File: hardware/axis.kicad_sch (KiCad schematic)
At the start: 43 parts, among them J101 Cortex_Debug, J102 DX07S016JA3, SW101 SKSG, SW102 SKSG, U101 TPS78433QWDRBRQ1, U102 ATSAMD51G, U103 BMM150, U104 BHI160, Y101 32k768

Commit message: Refresh
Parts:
- C102, C103, C104, C105, C111: Rating (none) -> 50V
- D103: Mouser 755-SML-D12M8WT86C -> 755-SML-D12D1WT86; Product SML-D12M8WT86C -> SML-D12D1WT86
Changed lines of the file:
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@@
 			)
 		)
+		(property "Rating" "50V"
+			(at 115.57 46.99 0)
+			(effects
+				(font
+					(size 1.27 1.27)
+				)
+				(hide yes)
+			)
+		)
 		(pin "1"
 		)
@@
 			)
 		)
+		(property "Rating" "50V"
+			(at 148.59 187.96 0)
+			(effects
+				(font
+					(size 1.27 1.27)
+				)
+				(hide yes)
+			)
+		)
 		(pin "1"
 		)
@@
 			)
 		)
-		(property "Mouser" "755-SML-D12M8WT86C"
+		(property "Mouser" "755-SML-D12D1WT86"
 			(at 254 97.536 0)
 			(effects
@@
 			)
 		)
-		(property "Product" "SML-D12M8WT86C "
+		(property "Product" "SML-D12D1WT86"
 			(at 127 41.91 0)
 			(effects
@@
 		(at 205.74 157.48 90)
 		(unit 1)
-		(exclude_from_sim no)
+		(exclude_from_sim yes)
 		(in_bom no)
 		(on_board yes)
@@
 			)
 		)
+		(property "Sim.Enable" "0"
+			(at 205.74 157.48 0)
+			(effects
+				(font
+					(size 1.27 1.27)
+				)
+				(hide yes)
+			)
+		)
 		(instances
 			(project "axis"
@@
 		(at 254 151.13 0)
 		(unit 1)
-		(exclude_from_sim no)
+		(exclude_from_sim yes)
 		(in_bom no)
 		(on_board yes)
@@
 			)
 		)
+		(property "Sim.Enable" "0"
+			(at 254 151.13 0)
+			(effects
+				(font
+					(size 1.27 1.27)
+				)
+				(hide yes)
+			)
+		)
 		(instances
 			(project ""
@@
 		(at 125.73 101.6 0)
 		(unit 1)
-		(exclude_from_sim no)
+		(exclude_from_sim yes)
 		(in_bom no)
 		(on_board yes)
@@
 			)
 		)
+		(property "Sim.Enable" "0"
+			(at 125.73 101.6 0)
+			(effects
+				(font
+					(size 1.27 1.27)
+				)
+				(hide yes)
+			)
+		)
 		(pin "1"
 		)
@@
 			)
 		)
-		(property "Description" "Power symbol creates a global label with name \"Earth\""
+		(property "Description" "Power symbol creates a global label with name \"Shield\""
 			(at 179.07 125.73 0)
 			(effects
@@
 			)
 		)
-		(property "Description" "Power symbol creates a global label with name \"Earth\""
+		(property "Description" "Power symbol creates a global label with name \"Shield\""
 			(at 238.76 81.28 0)
 			(effects
@@
 			)
 		)
+		(property "Rating" "50V"
+			(at 105.41 46.99 0)
+			(effects
+				(font
+					(size 1.27 1.27)
+				)
+				(hide yes)
+			)
+		)
 		(pin "1"
 		)
@@
 			)
 		)
+		(property "Rating" "50V"
+			(at 85.09 46.99 0)
+			(effects
+				(font
+					(size 1.27 1.27)
+				)
+				(hide yes)
+			)
+		)
 		(pin "1"
 		)
@@
 		(at 254 158.75 0)
 		(unit 1)
-		(exclude_from_sim no)
+		(exclude_from_sim yes)
 		(in_bom no)
 		(on_board yes)
@@
 			)
 		)
+		(property "Sim.Enable" "0"
+			(at 254 158.75 0)
+			(effects
+				(font
+					(size 1.27 1.27)
+				)
+				(hide yes)
+			)
+		)
 		(instances
 			(project "axis"
@@
 			)
 		)
+		(property "Rating" "50V"
+			(at 95.25 46.99 0)
+			(effects
+				(font
+					(size 1.27 1.27)
+				)
+				(hide yes)
+			)
+		)
 		(pin "1"
 		)
@@
 		(at 179.07 175.26 0)
 		(unit 1)
-		(exclude_from_sim no)
+		(exclude_from_sim yes)
 		(in_bom no)
 		(on_board yes)
@@
 			)
 		)
+		(property "Sim.Enable" "0"
+			(at 179.07 175.26 0)
+			(effects
+				(font
+					(size 1.27 1.27)
+				)
+				(hide yes)
+			)
+		)
 		(instances
 			(project "axis"
@@
 		(at 180.34 156.21 0)
 		(unit 1)
-		(exclude_from_sim no)
+		(exclude_from_sim yes)
 		(in_bom no)
 		(on_board yes)
@@
 			(at 180.34 156.21 0)
 			(effects
+				(font
+					(size 1.27 1.27)
+				)
+				(hide yes)
+			)
+		)
+		(property "Sim.Enable" "0"
+			(at 180.34 156.21 0)
+			(effects

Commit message: Refresh
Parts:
- C101, C110: Rating (none) -> 10V
- C102, C103, C104, C105, C111: Manufacturer YAGEO -> TDK; Mouser 603-CC603KRX7R9BB105 -> 810-CGA3E3X7R1H105K0; Product CC0603KRX7R9BB105 -> CGA3E3X7R1H105K080AB

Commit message: Update library
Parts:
- J101: value Cortex_Debug -> Cortex; footprint V2_Cortex_Debug:Cortex_Debug_Pad -> V2_Connector_Debug:Cortex; symbol V2_Cortex_Debug:Cortex_Debug -> V2_Connector_Debug:Cortex
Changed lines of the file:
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@@
 	)
 	(symbol
-		(lib_id "V2_Cortex_Debug:Cortex_Debug")
+		(lib_id "V2_Connector_Debug:Cortex")
 		(at 125.73 101.6 0)
 		(unit 1)
@@
 			)
 		)
-		(property "Value" "Cortex_Debug"
+		(property "Value" "Cortex"
 			(at 127 91.44 0)
 			(effects
@@
 			)
 		)
-		(property "Footprint" "V2_Cortex_Debug:Cortex_Debug_Pad"
+		(property "Footprint" "V2_Connector_Debug:Cortex"
 			(at 125.73 115.57 0)
 			(effects

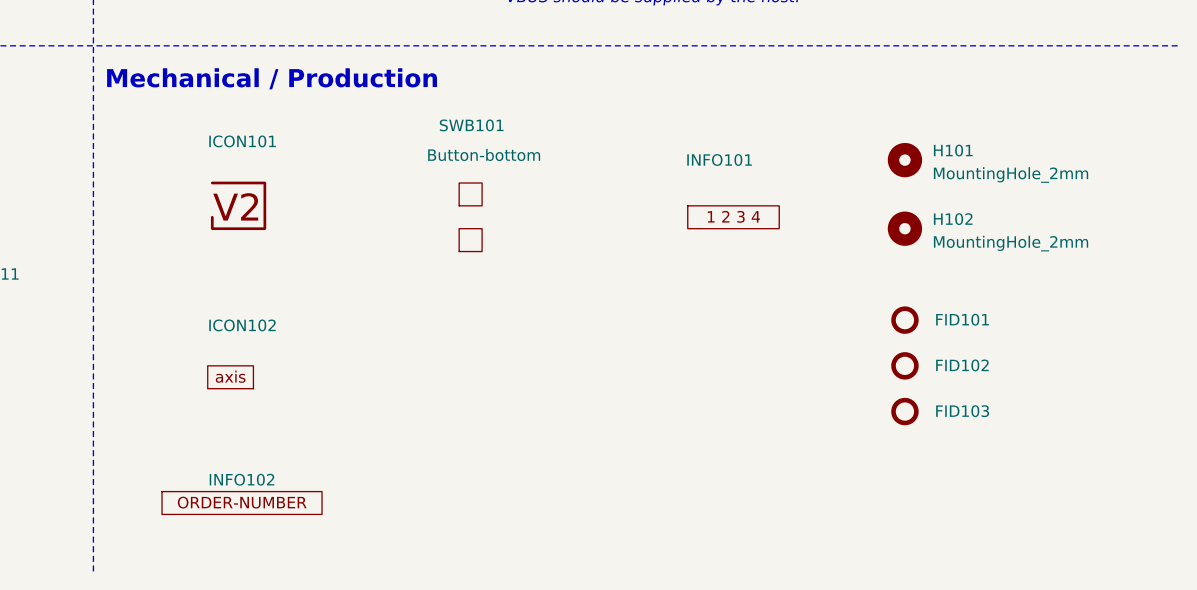
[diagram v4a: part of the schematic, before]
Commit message: Replace Order_Number
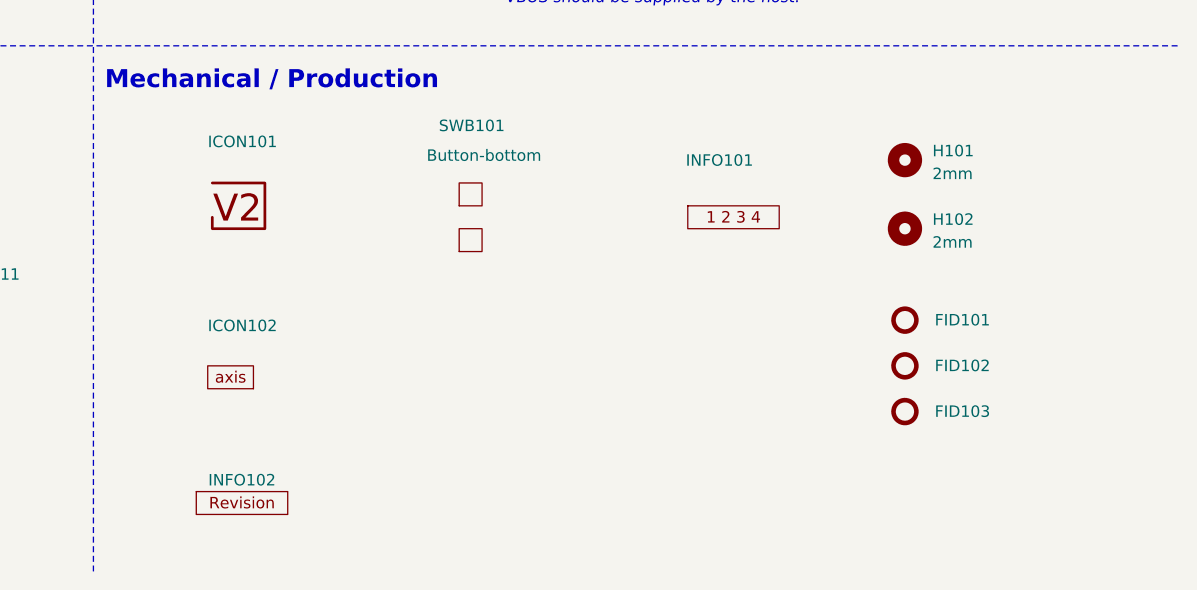
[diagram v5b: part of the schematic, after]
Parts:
- H101, H102: value MountingHole_2mm -> 2mm
- INFO102: value Order_Number -> ~; footprint V2_Production:Order_Number -> V2_Production:Revision; symbol V2_Production:Order_Number -> V2_Production:Revision
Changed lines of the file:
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@@
 		(at 205.74 157.48 90)
 		(unit 1)
-		(exclude_from_sim yes)
+		(exclude_from_sim no)
 		(in_bom no)
 		(on_board yes)
@@
 			)
 		)
+		(property "Sim.Enable" "0"
+			(at 205.74 157.48 0)
+			(effects
+				(font
+					(size 1.27 1.27)
+				)
+				(hide yes)
+			)
+		)
 		(instances
 			(project "axis"
@@
 		(at 254 151.13 0)
 		(unit 1)
-		(exclude_from_sim yes)
+		(exclude_from_sim no)
 		(in_bom no)
 		(on_board yes)
@@
 			)
 		)
-		(property "Value" "MountingHole_2mm"
+		(property "Value" "2mm"
 			(at 257.048 152.654 0)
 			(effects
@@
 	)
 	(symbol
-		(lib_id "V2_Production:Order_Number")
+		(lib_id "V2_Production:Revision")
 		(at 180.34 189.23 0)
 		(unit 1)
@@
 			)
 		)
-		(property "Value" "Order_Number"
+		(property "Value" "~"
 			(at 180.34 191.77 0)
 			(effects
@@
 			)
 		)
-		(property "Footprint" "V2_Production:Order_Number"
+		(property "Footprint" "V2_Production:Revision"
 			(at 180.34 194.31 0)
 			(effects
@@
 		(at 254 158.75 0)
 		(unit 1)
-		(exclude_from_sim yes)
+		(exclude_from_sim no)
 		(in_bom no)
 		(on_board yes)
@@
 			)
 		)
-		(property "Value" "MountingHole_2mm"
+		(property "Value" "2mm"
 			(at 257.048 160.274 0)
 			(effects
@@
 		(at 179.07 175.26 0)
 		(unit 1)
-		(exclude_from_sim yes)
+		(exclude_from_sim no)
 		(in_bom no)
 		(on_board yes)
@@
 			)
 		)
+		(property "Sim.Enable" "0"
+			(at 179.07 175.26 0)
+			(effects
+				(font
+					(size 1.27 1.27)
+				)
+				(hide yes)
+			)
+		)
 		(instances
 			(project "axis"
@@
 		(at 180.34 156.21 0)
 		(unit 1)
-		(exclude_from_sim yes)
+		(exclude_from_sim no)
 		(in_bom no)
 		(on_board yes)

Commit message: Update Library
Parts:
- C101, C110: symbol V2_Device:C_0603_10u -> V2_Capacitor:0603_10u
- C102, C103, C104, C105, C111: symbol V2_Device:C_0603_1u -> V2_Capacitor:0603_1u
- C106, C107: symbol V2_Device:C_0805_10u -> V2_Capacitor:0805_10u
- C108, C109: symbol V2_Device:C_0603_18p -> V2_Capacitor:0603_18p
- C112: symbol V2_Device:C_0603_0u47 -> V2_Capacitor:0603_0u47
- D103: symbol V2_Device:LED_0603_Orange -> V2_LED:0603_Orange
- R101: symbol V2_Device:R_0603_330R -> V2_Resistor:0603_330R
- R102, R103: symbol V2_Device:R_0603_5k1 -> V2_Resistor:0603_5k1
- R104: symbol V2_Device:R_0603_100k -> V2_Resistor:0603_100k
- R105, R106, R107, R108: symbol V2_Device:R_0603_2k7 -> V2_Resistor:0603_2k7
- Y101: symbol V2_Device:Crystal_3.2x1.5_32k768 -> V2_Crystal:3.2x1.5_32k768

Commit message: Update
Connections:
- net Aux-SCK renamed Aux-SCL
- net SCK renamed SCL
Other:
- moved on the sheet: FID101, FID102, FID103, H101, H102, ICON101, ICON102, INFO101, INFO102, SWB101

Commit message: Export stencil
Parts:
- INFO102: value ~ -> (none)
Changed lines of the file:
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@@
 	(title_block
 		(title "V2 axis")
-		(date "2026-02-10")
+		(date "2026-02-25")
 		(rev "2026-01-14")
 		(company "Versio Duo")
@@
 		(at 234.95 152.4 90)
 		(unit 1)
-		(exclude_from_sim yes)
+		(exclude_from_sim no)
 		(in_bom no)
 		(on_board yes)
@@
 			)
 		)
+		(property "Sim.Enable" "0"
+			(at 234.95 152.4 0)
+			(effects
+				(font
+					(size 1.27 1.27)
+				)
+				(hide yes)
+			)
+		)
 		(instances
 			(project "axis"
@@
 			)
 		)
-		(property "Value" "~"
+		(property "Value" ""
 			(at 176.53 175.26 0)
 			(effects
@@
 		(at 176.53 165.1 0)
 		(unit 1)
-		(exclude_from_sim yes)
+		(exclude_from_sim no)
 		(in_bom no)
 		(on_board yes)
@@
 			(at 176.53 165.1 0)
 			(effects
+				(font
+					(size 1.27 1.27)
+				)
+				(hide yes)
+			)
+		)
+		(property "Sim.Enable" "0"
+			(at 176.53 165.1 0)
+			(effects
